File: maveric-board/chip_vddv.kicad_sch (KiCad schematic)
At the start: 17 parts, among them U1 Socket

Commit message: add fmc lpc symbol
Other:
- title: (none) -> Maveric Board
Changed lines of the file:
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@@
 	(paper "A4")
 	(title_block
-		(date "2024-06-09")
+		(title "Maveric Board")
+		(date "2024-06-10")
 		(rev "0")
+		(comment 1 "Drawn By: Vighnesh Iyer")
 	)
 	(junction

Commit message: add jlcpcb 10u cap part + footprint
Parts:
- C17, C18, C19, C20, C21, C22, C23, C24, C25, C26, C27, C28, C29, C30, C31, C32: footprint (none) -> Capacitor_SMD:C_0603_1608Metric; JLCPCB Part # (none) -> C95839

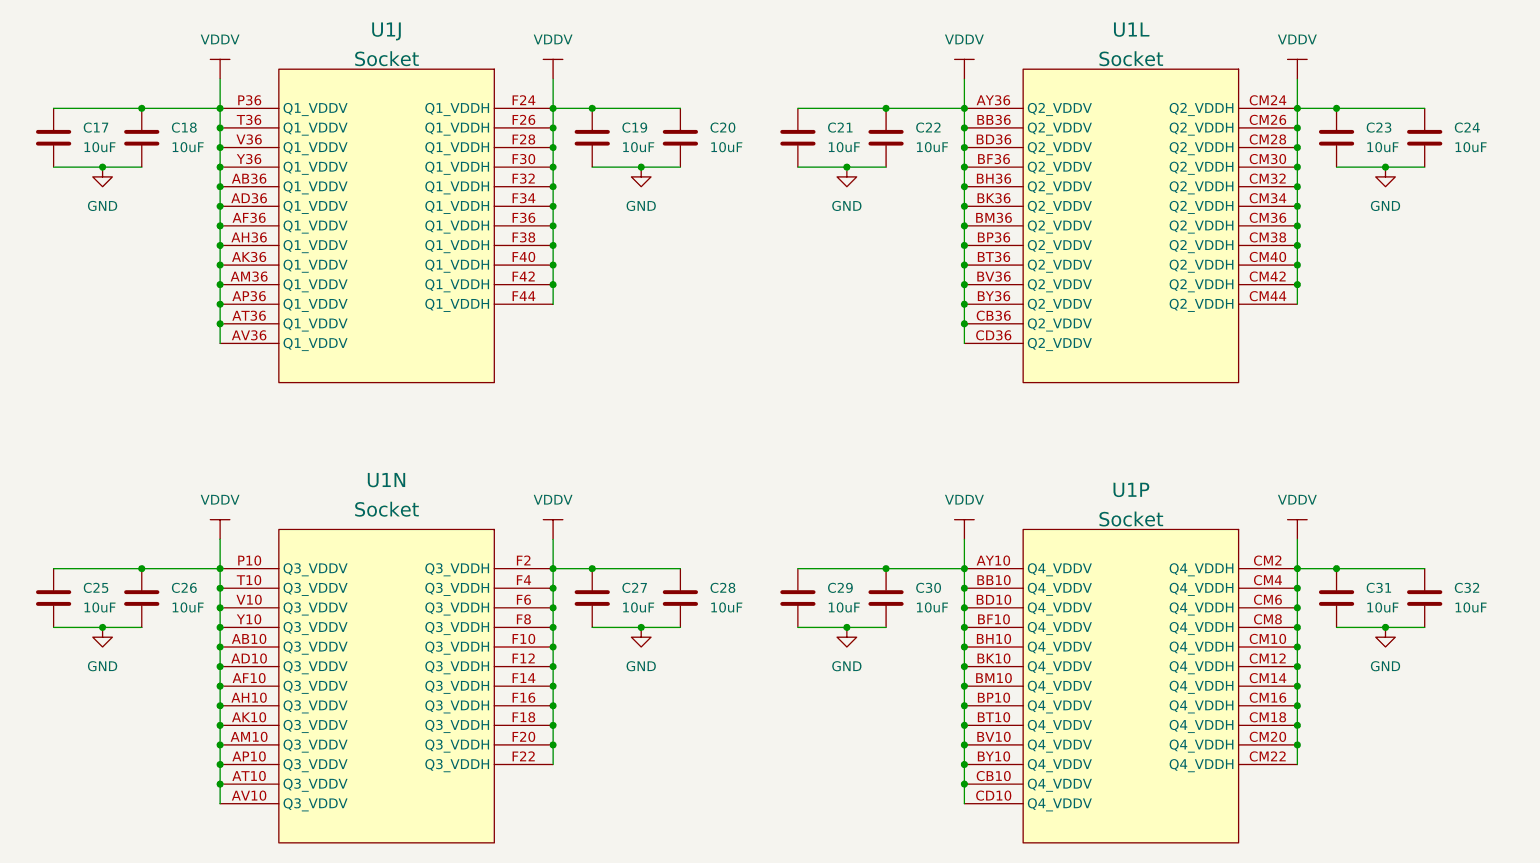
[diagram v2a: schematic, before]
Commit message: reannotate, fix all ERCs
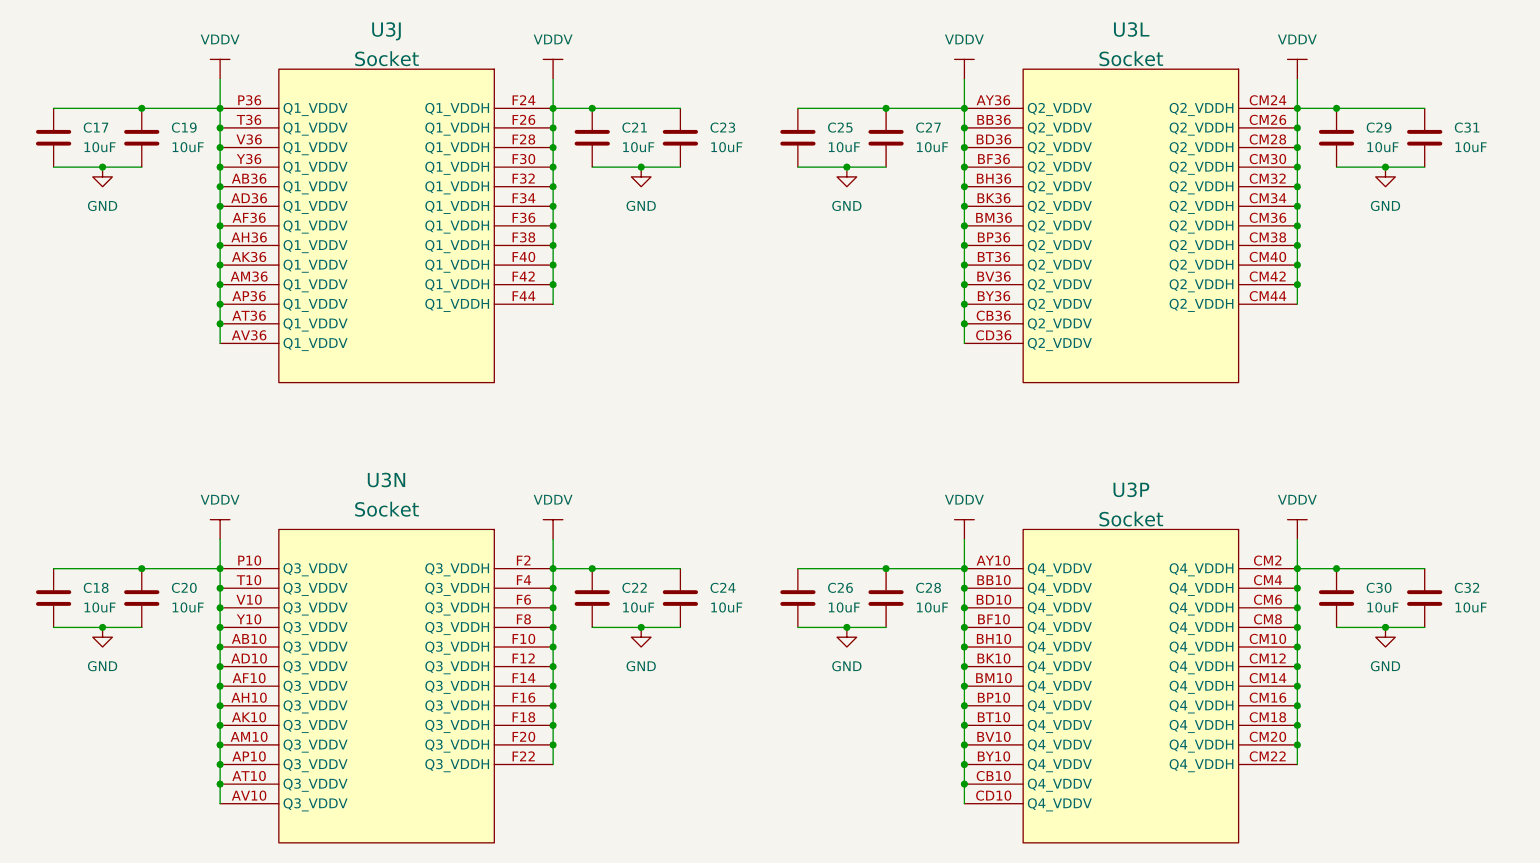
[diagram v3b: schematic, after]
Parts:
- renumbered C25 to C18, C18 to C19, C26 to C20, C19 to C21, C27 to C22, C20 to C23, C28 to C24, C21 to C25, C29 to C26, C22 to C27, C30 to C28, C23 to C29, C31 to C30, C24 to C31, U1 to U3

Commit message: add uni2 socket footprint, check against drawing, fix npth, assign all footprints and part numbers
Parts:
- U3: footprint (none) -> maveric-parts:BGA-1733-.92-47.725x47.725
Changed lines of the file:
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@@
 			)
 		)
-		(property "Footprint" ""
+		(property "Footprint" "maveric-parts:BGA-1733-.92-47.725x47.725"
 			(at 130.81 21.59 0)
 			(effects
@@
 			)
 		)
-		(property "Footprint" ""
+		(property "Footprint" "maveric-parts:BGA-1733-.92-47.725x47.725"
 			(at 34.29 81.28 0)
 			(effects
@@
 			)
 		)
-		(property "Footprint" ""
+		(property "Footprint" "maveric-parts:BGA-1733-.92-47.725x47.725"
 			(at 34.29 21.59 0)
 			(effects
@@
 			)
 		)
-		(property "Footprint" ""
+		(property "Footprint" "maveric-parts:BGA-1733-.92-47.725x47.725"
 			(at 130.81 81.28 0)
 			(effects

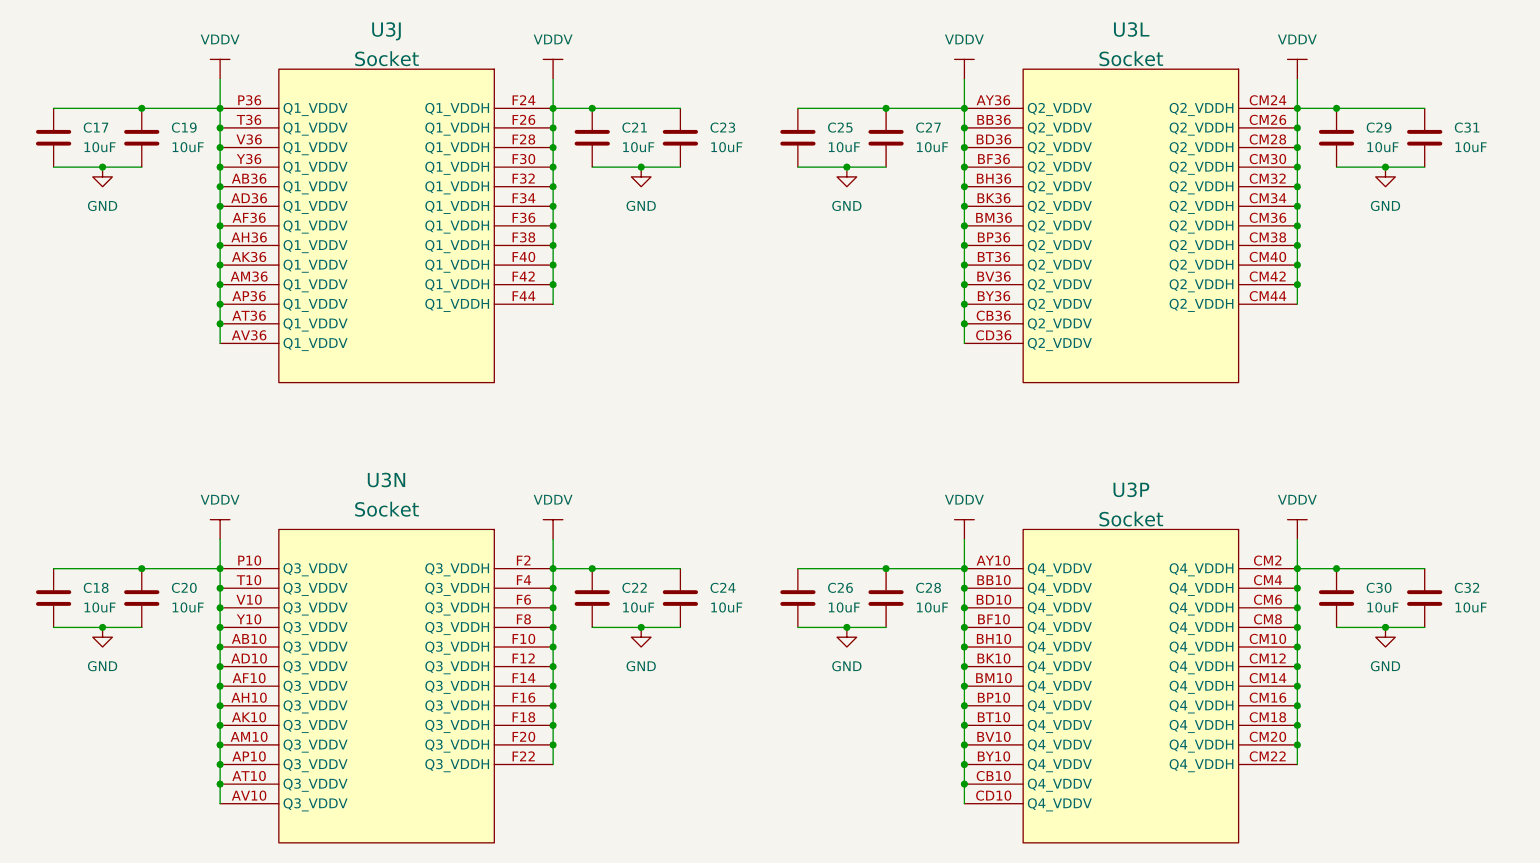
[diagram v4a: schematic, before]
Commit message: add testpoint for pg_c2m and fixup footprints for led and mosfet with correct pin mapping
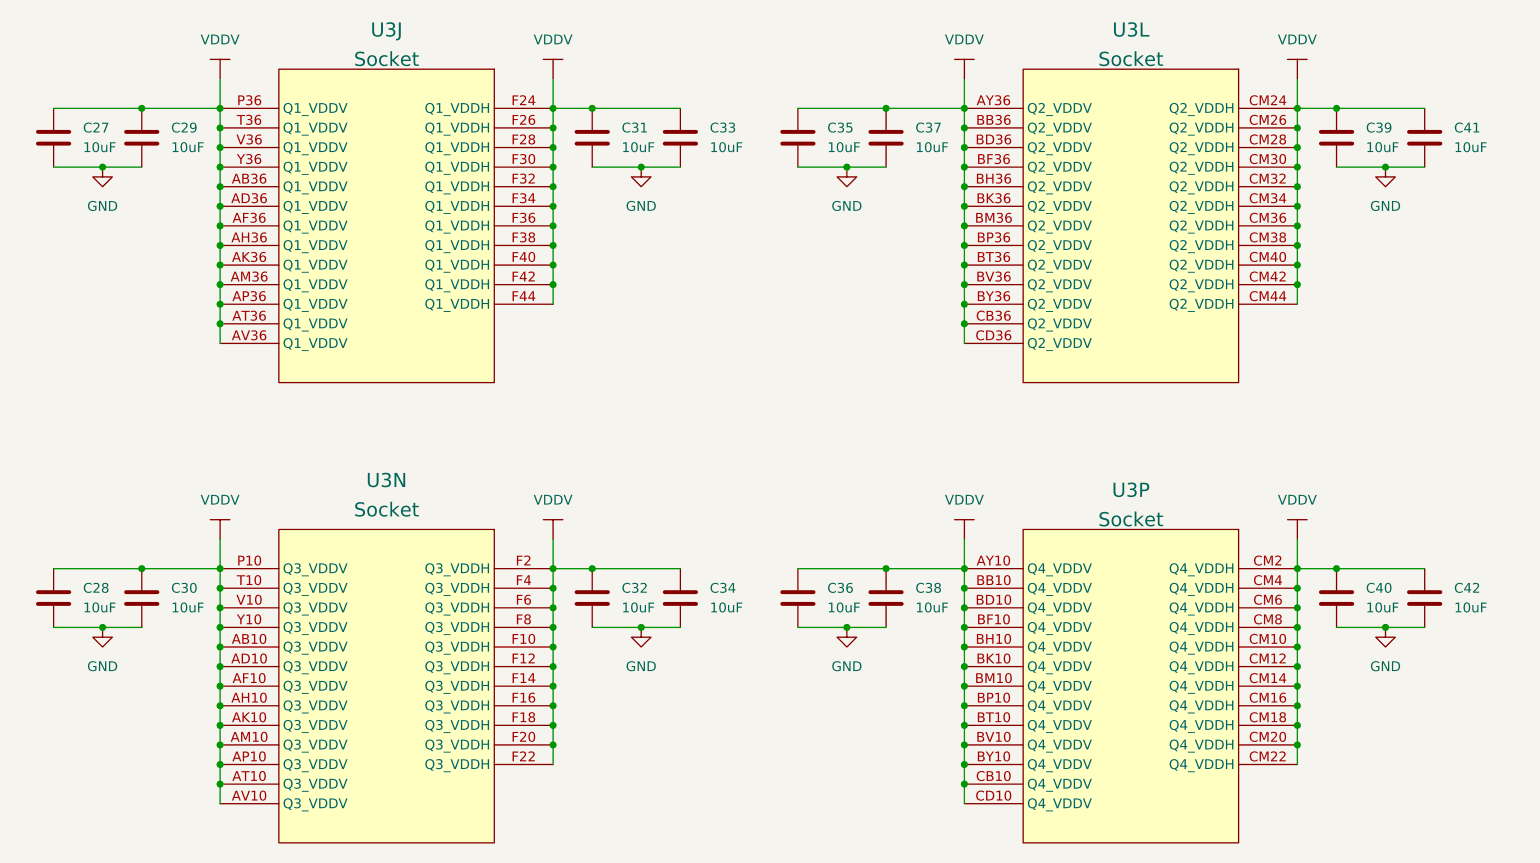
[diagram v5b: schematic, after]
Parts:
- renumbered C17 to C27, C18 to C28, C19 to C29, C20 to C30, C21 to C31, C22 to C32, C23 to C33, C24 to C34, C25 to C35, C26 to C36, C27 to C37, C28 to C38, C29 to C39, C30 to C40, C31 to C41, C32 to C42

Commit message: some docs + dnp uni2 socket
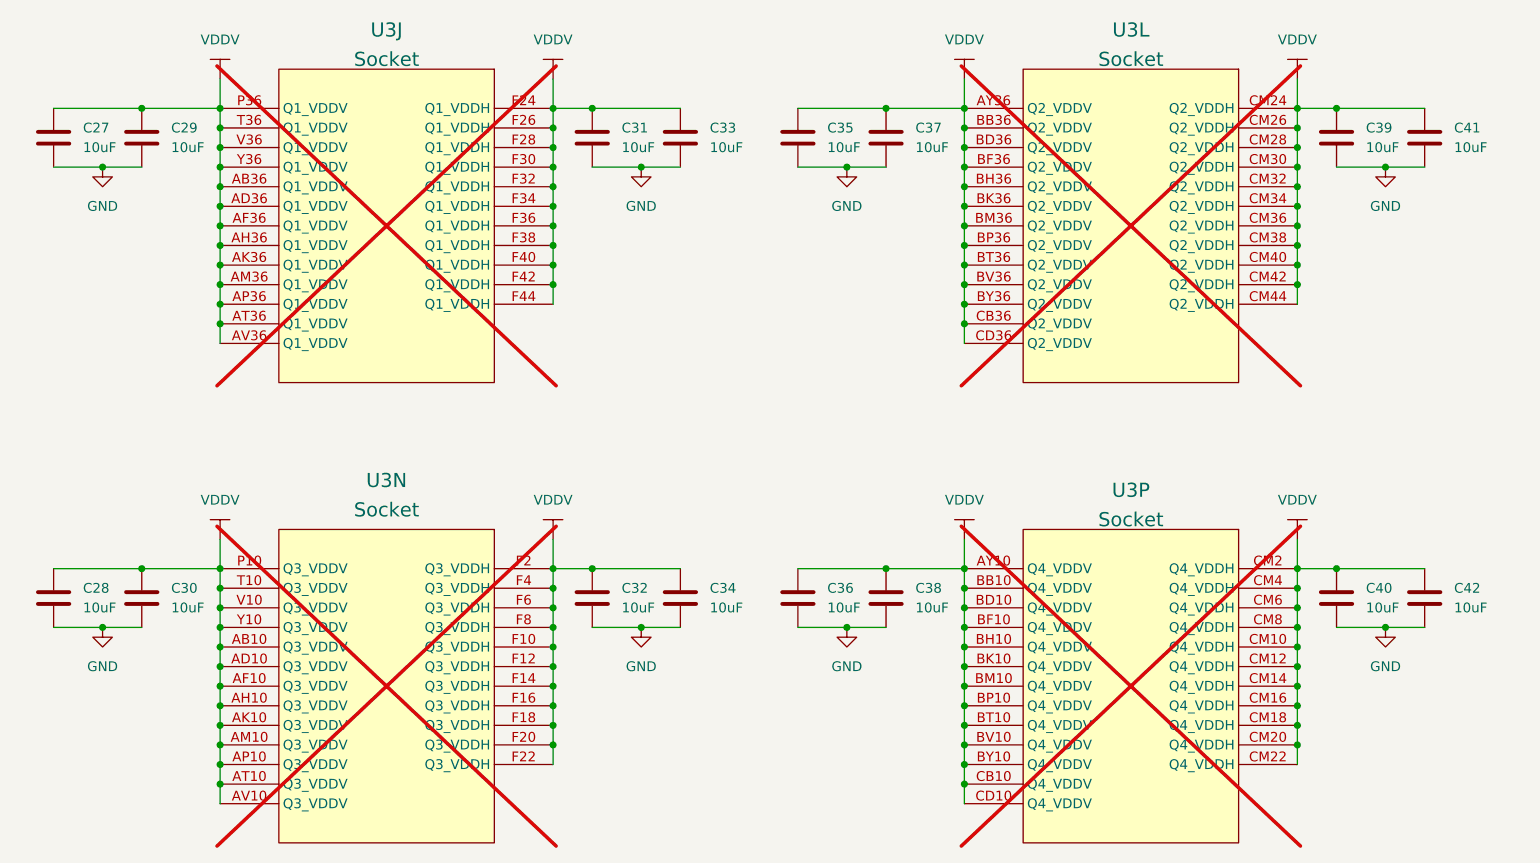
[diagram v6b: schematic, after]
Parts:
- U3: now not fitted
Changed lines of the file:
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@@
 		(in_bom yes)
 		(on_board yes)
-		(dnp no)
+		(dnp yes)
 		(fields_autoplaced yes)
 		(property "Reference" "U3"
@@
 		(in_bom yes)
 		(on_board yes)
-		(dnp no)
+		(dnp yes)
 		(fields_autoplaced yes)
 		(property "Reference" "U3"
@@
 		(in_bom yes)
 		(on_board yes)
-		(dnp no)
+		(dnp yes)
 		(fields_autoplaced yes)
 		(property "Reference" "U3"
@@
 		(in_bom yes)
 		(on_board yes)
-		(dnp no)
+		(dnp yes)
 		(fields_autoplaced yes)
 		(property "Reference" "U3"

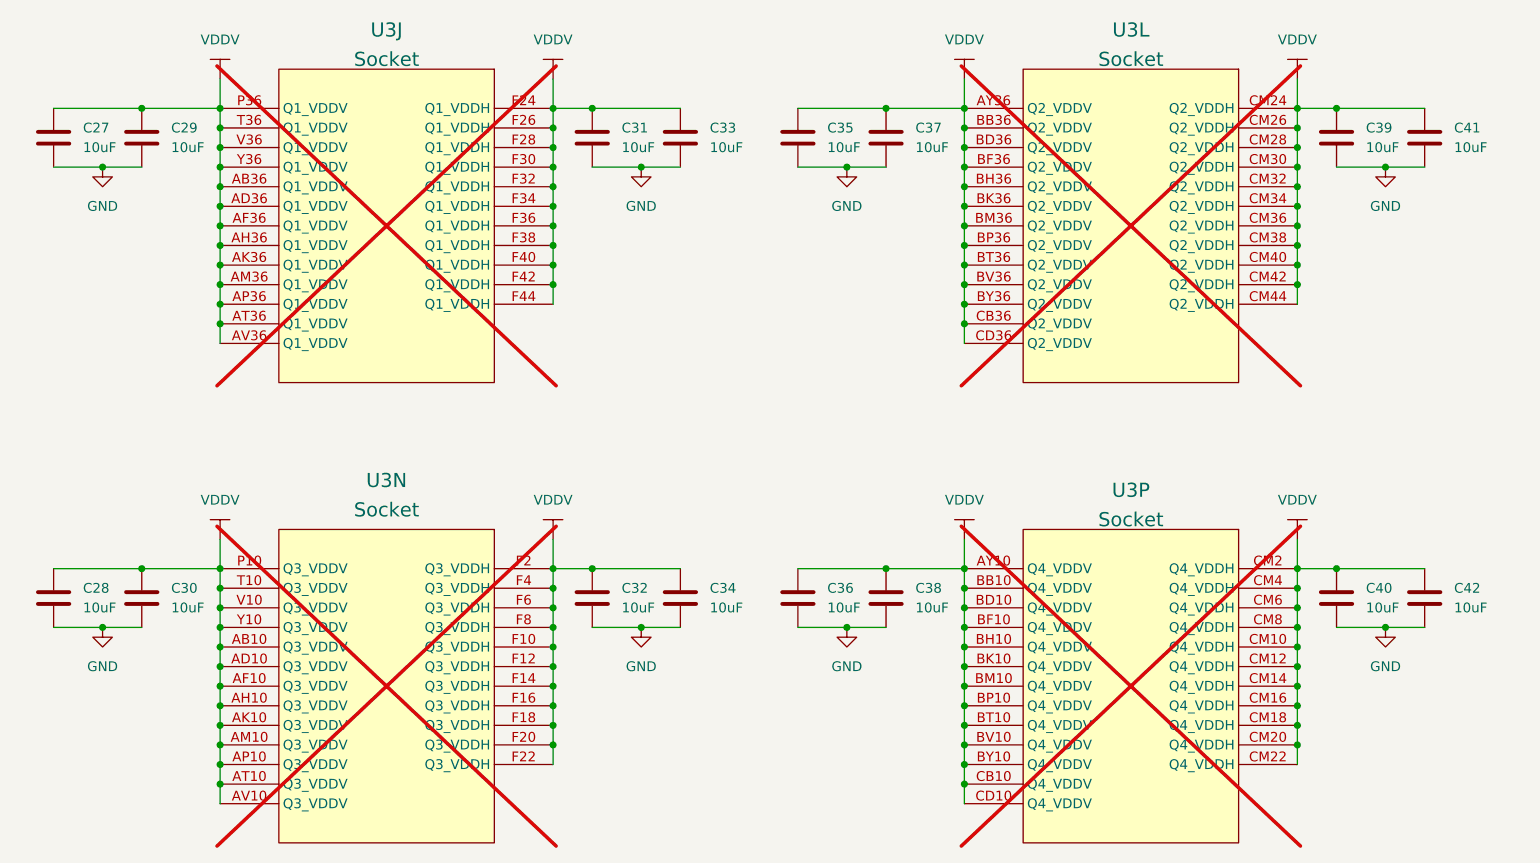
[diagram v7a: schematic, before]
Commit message: add mfr part # attribute to each symbol, resync board layout, remove excess VDDV decap
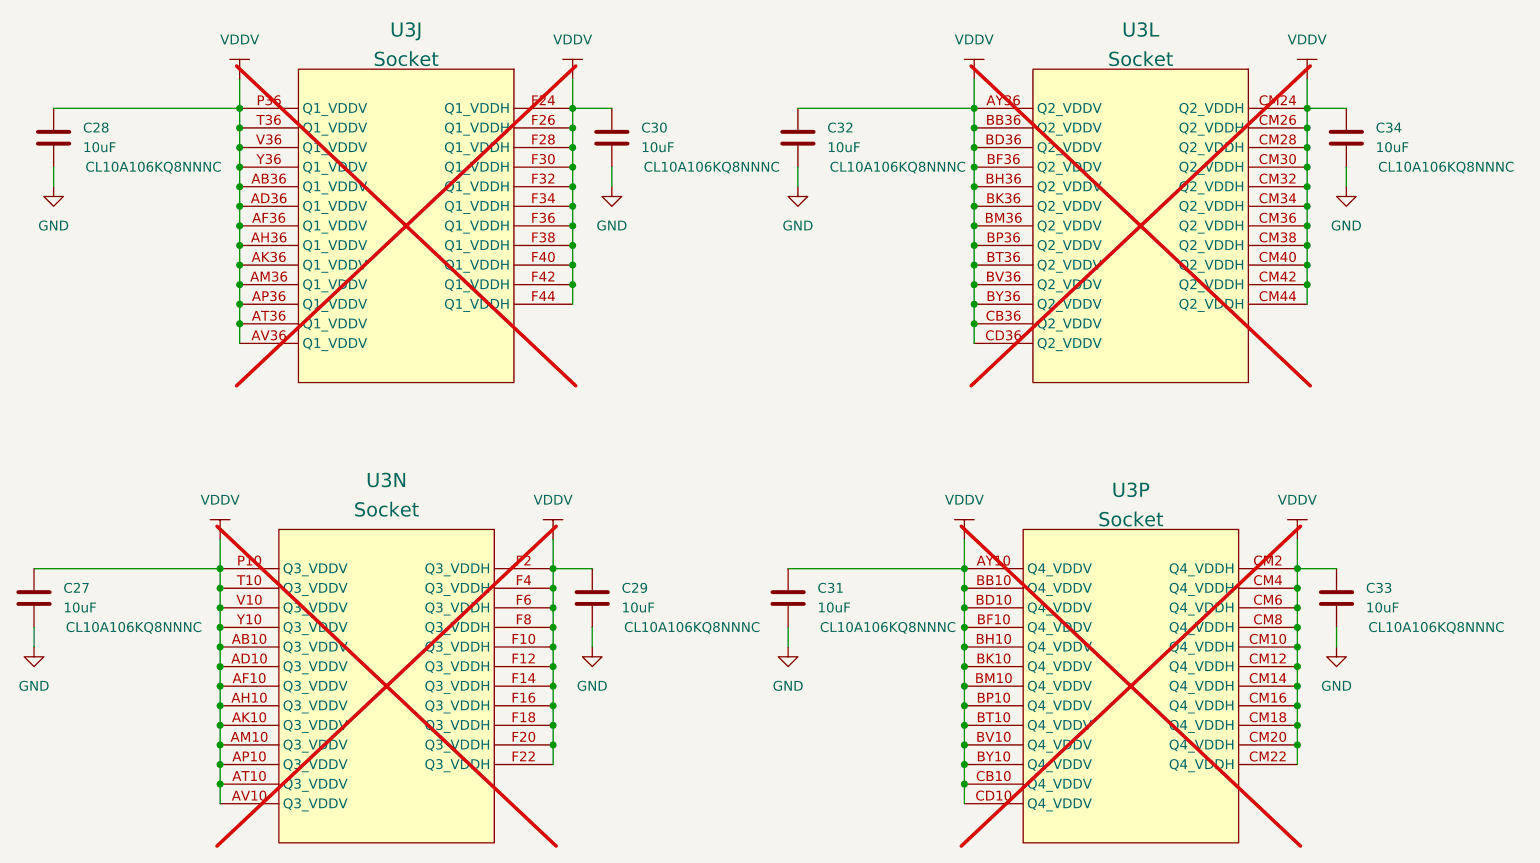
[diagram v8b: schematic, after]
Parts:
- removed C28, C35, C36, C37, C38, C39, C40, C41, C42: 10uF, Capacitor_SMD:C_0603_1608Metric, symbol Device:C
- added C27: 10uF, Capacitor_SMD:C_0603_1608Metric, symbol Device:C
- C28: renamed from C27; Mfr Part # (none) -> CL10A106KQ8NNNC
- C29, C30, C31, C32, C33, C34: Mfr Part # (none) -> CL10A106KQ8NNNC
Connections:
- net GND: now also C27.2
- net VDDV: now also C27.1
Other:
- moved on the sheet: U3J, U3L
